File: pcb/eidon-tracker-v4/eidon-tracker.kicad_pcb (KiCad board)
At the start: 2 copper layers, 29.5 x 24.2 mm, 13 parts, among them SW1 SW_SPDT, U1 XIAO-ESP32C6-SMD, U2 BNO085

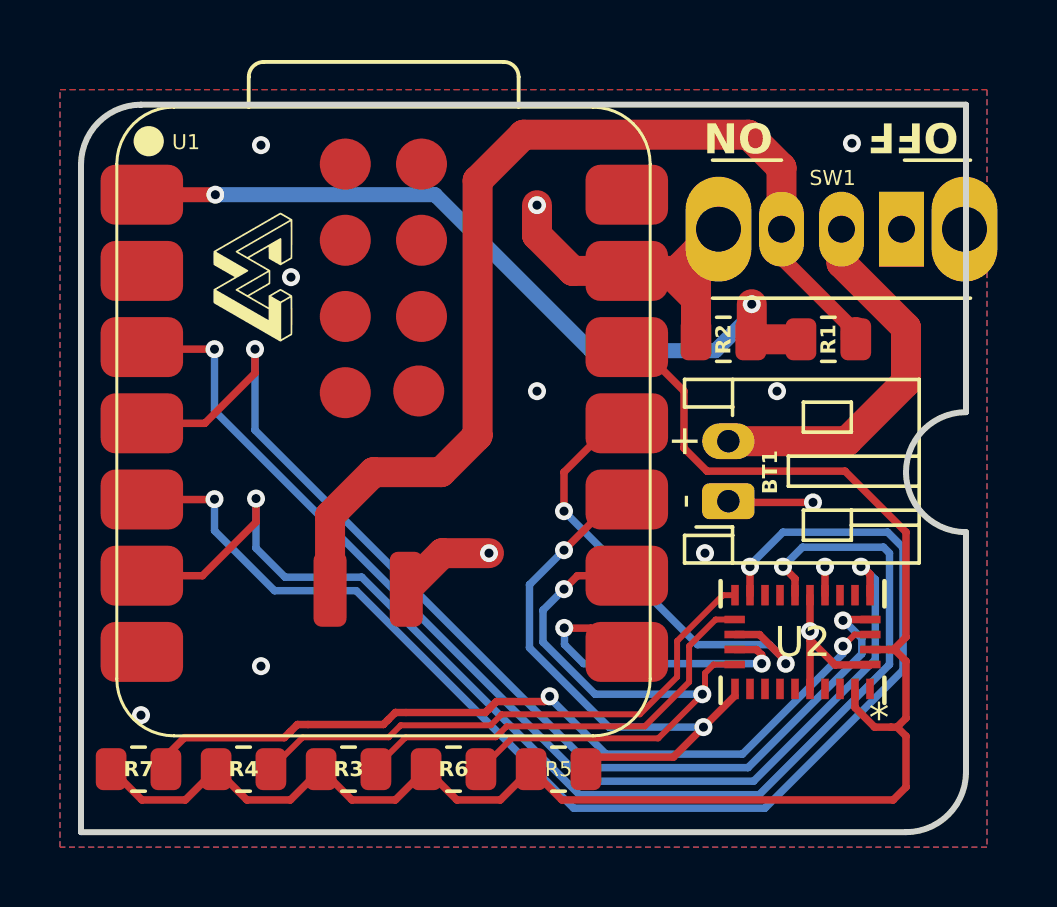
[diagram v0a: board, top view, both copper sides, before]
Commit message: feat(pcb): further refining traces for bno085 chip layout
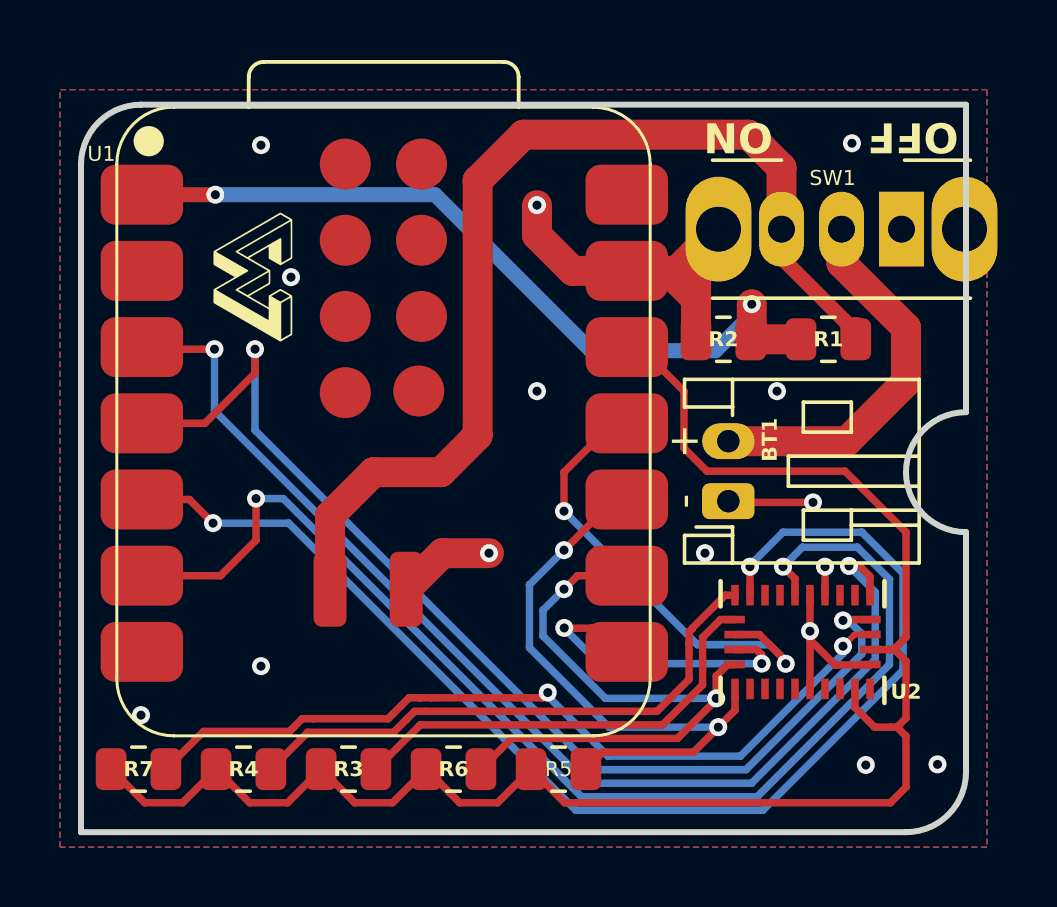
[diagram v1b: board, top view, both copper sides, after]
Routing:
- net /RST: track 42.1 -> 41.0 mm
- net /INT: track 43.0 -> 42.0 mm
- net /MISO: track 19.6 -> 20.4 mm
- net /SCK: track 20.7 -> 21.4 mm
- net /PS0: track 37.7 -> 38.3 mm
- net GND: vias 12 -> 14

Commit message: fix(pcb): corrects component placement so not too close to edge per jlcpcb rejection feedback
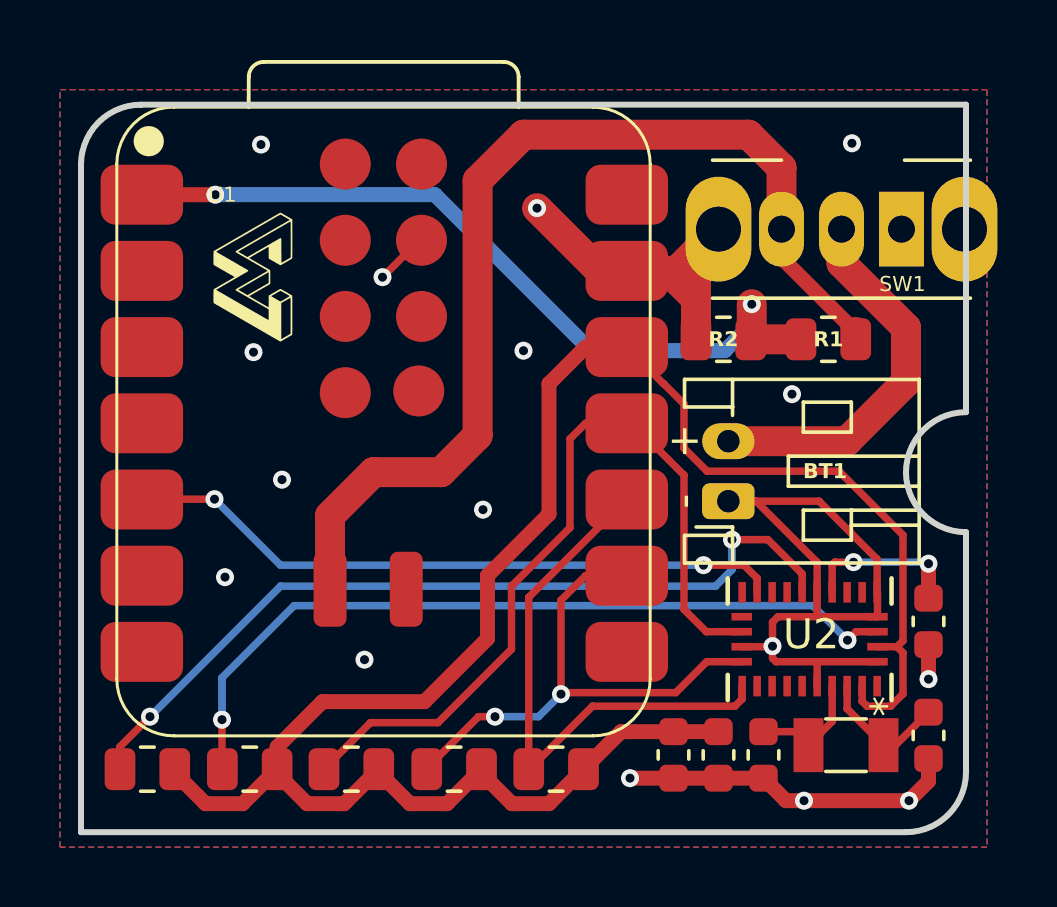
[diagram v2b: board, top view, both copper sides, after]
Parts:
- added C1: 22pF, Capacitor_SMD:C_0603_1608Metric, F.Cu at (162.2, 108.3)
- added C2: 22pF, Capacitor_SMD:C_0603_1608Metric, F.Cu at (156.8, 108.9)
- added C3: 100nF, Capacitor_SMD:C_0603_1608Metric, F.Cu at (162.2, 104.5)
- added C4: 100nF, Capacitor_SMD:C_0603_1608Metric, F.Cu at (155.2, 108.9)
- added C5: 100nF, Capacitor_SMD:C_0603_1608Metric, F.Cu at (153.8, 108.9)
- added X1: 32.768KHz, Crystal:Crystal_SMD_3215-2Pin_3.2x1.5mm, F.Cu at (159.5, 108.6)
- R5, R6: value 2.2k -> 10k
- U1: value XIAO-ESP32C6-SMD -> XIAO-ESP32-C6
- U2: footprint eidon-tracker:LGA-28_CEV -> eidon-tracker:BNO085
- moved R4 10.4 mm to (149.8, 109.4), turned to 0 degrees
- moved R5 10.3 mm to (139.6, 109.4), turned to 0 degrees
- moved R6 10.2 mm to (136.2, 109.4), turned to 0 degrees
- moved R7 7.10 mm to (143.0, 109.4), turned to 0 degrees
- moved R3 3.52 mm to (146.4, 109.4), turned to 0 degrees
- moved U2 0.26 mm to (158.3, 105.1)
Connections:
- R3 pad 1: Net-(U2-ENV_SDA) -> /SCL
- R4 pad 1: Net-(U2-ENV_SCL) -> /SDA
- R5 pad 1: /MISO -> /BOOTN
- R6 pad 1: /SCK -> /RST
- R7 pad 1: /BOOTN -> /SDO
- U1 pad 10: /MISO -> /SDA
- U1 pad 11: /MOSI -> /SDO
- U1 pad 14: (no net) -> unconnected-(U1-5V-Pad14)
- U1 pad 17: (no net) -> unconnected-(U1-MTDI-Pad17)
- U1 pad 18: (no net) -> unconnected-(U1-MTDO-Pad18)
- U1 pad 19: (no net) -> unconnected-(U1-EN-Pad19)
- U1 pad 20: (no net) -> GND
- U1 pad 21: (no net) -> unconnected-(U1-MTMS-Pad21)
- U1 pad 22: (no net) -> unconnected-(U1-MTCK-Pad22)
- U1 pad 23: /BOOT -> unconnected-(U1-BOOT-Pad23)
- U1 pad 24: (no net) -> unconnected-(U1-3V3_1-Pad24)
- U1 pad 3: /PS0 -> unconnected-(U1-GPIO2_A2_D2-Pad3)
- U1 pad 4: /PS1 -> unconnected-(U1-GPIO21_D3-Pad4)
- U1 pad 6: /RST -> unconnected-(U1-GPIO23_D5_SCL-Pad6)
- U1 pad 7: (no net) -> unconnected-(U1-GPIO16_D6_TX-Pad7)
- U1 pad 8: /CS -> unconnected-(U1-GPIO17_D7_RX-Pad8)
- U1 pad 9: /SCK -> /SCL
- U2 pad 15: Net-(U2-ENV_SCL) -> unconnected-(U2-ENV_SCL-Pad15)
- U2 pad 16: Net-(U2-ENV_SDA) -> unconnected-(U2-ENV_SDA-Pad16)
- U2 pad 17: /MOSI -> /SDO
- U2 pad 18: /CS -> GND
- U2 pad 19: /SCK -> /SCL
- U2 pad 20: /MISO -> /SDA
- U2 pad 26: unconnected-(U2-XOUT32/CLKSEL1-Pad26) -> /XOUT
- U2 pad 27: unconnected-(U2-XIN32-Pad27) -> /XIN
- U2 pad 5: /PS1 -> GND
- U2 pad 6: /PS0 -> GND
- U2 pad 9: unconnected-(U2-CAP-Pad9) -> /CAP
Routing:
- net /PS0: track 38.3 -> 0.00 mm, vias 2 -> 0
- net /PS1: track 37.0 -> 0.00 mm, vias 2 -> 0
- net /SDO: track 0.00 -> 27.3 mm
- net GND: track 28.0 -> 53.9 mm, vias 14 -> 16
- net /SCK: track 21.4 -> 0.00 mm, vias 2 -> 0
- net /MISO: track 20.4 -> 0.00 mm, vias 2 -> 0
- net /INT: track 42.0 -> 22.1 mm
- net /SDA: track 0.00 -> 18.9 mm
- net Net-(U2-ENV_SCL): track 18.8 -> 0.00 mm
- net /SCL: track 0.00 -> 18.0 mm, vias 0 -> 2
- net /MOSI: track 16.0 -> 0.00 mm, vias 2 -> 0
- net Net-(U2-ENV_SDA): track 15.0 -> 0.00 mm
- net /RST: track 41.0 -> 28.0 mm
- net /CS: track 10.9 -> 0.00 mm, vias 2 -> 0
- net VCC: track 56.2 -> 65.3 mm
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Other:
- board text removed: "OFF"
- board text removed: "ON"

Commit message: chore(pcb): commits hanging changes with final PCB design changes
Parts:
- R1, R2: value 220k -> 220kΩ
- R3, R4: value 2.2k -> 2.2kΩ
- R5, R6, R7: value 10k -> 10kΩ
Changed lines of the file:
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@@
 	(setup
 		(pad_to_mask_clearance 0.05)
-		(solder_mask_min_width 0.05)
 		(allow_soldermask_bridges_in_footprints no)
 		(tenting front back)
@@
 			)
 		)
-		(property "Value" "10k"
+		(property "Value" "10kΩ"
 			(at 0 1.65 0)
 			(layer "F.Fab")
@@
 			)
 		)
-		(property "Datasheet" "BNO085"
-			(at 0 0 270)
+		(property "Datasheet" "https://www.ceva-ip.com/wp-content/uploads/BNO080_085-Datasheet.pdf"
+			(at 0 0 90)
 			(layer "F.Fab")
 			(hide yes)
@@
 			)
 		)
-		(property "Description" ""
-			(at 0 0 270)
+		(property "Description" "9-Axis IMU Sensor Hub LGA-28"
+			(at 0 0 90)
 			(layer "F.Fab")
 			(hide yes)
@@
 			)
 		)
+		(property "Manufacturer" "CEVA Technologies"
+			(at 0 0 0)
+			(unlocked yes)
+			(layer "F.Fab")
+			(hide yes)
+			(effects
+				(font
+					(size 1 1)
+					(thickness 0.15)
+				)
+			)
+		)
+		(property "Manufacturer Part Number (MPN)" "BNO085"
+			(at 0 0 0)
+			(unlocked yes)
+			(layer "F.Fab")
+			(hide yes)
+			(effects
+				(font
+					(size 1 1)
+					(thickness 0.15)
+				)
+			)
+		)
+		(property "Supplier" "DigiKey"
+			(at 0 0 0)
+			(unlocked yes)
+			(layer "F.Fab")
+			(hide yes)
+			(effects
+				(font
+					(size 1 1)
+					(thickness 0.15)
+				)
+			)
+		)
+		(property "Supplier_PN" "1888-1006-1-ND"
+			(at 0 0 0)
+			(unlocked yes)
+			(layer "F.Fab")
+			(hide yes)
+			(effects
+				(font
+					(size 1 1)
+					(thickness 0.15)
+				)
+			)
+		)
 		(property ki_fp_filters "LGA-28_CEV")
 		(sheetname "/")
@@
 		)
 		(fp_text user "*"
-			(at 2.2356 -2.2625 270)
+			(at 2.2356 -2.2625 90)
 			(layer "F.SilkS")
 			(hide yes)
@@
 		)
 		(fp_text user "*"
-			(at 1.143 -2.2606 270)
+			(at 1.143 -2.2606 90)
 			(layer "F.Fab")
 			(hide yes)
@@
 			)
 		)
-		(property "Value" "10k"
+		(property "Value" "10kΩ"
 			(at 0 1.65 0)
 			(layer "F.Fab")
@@
 			)
 		)
-		(property "Value" "220k"
+		(property "Value" "220kΩ"
 			(at 0 0 90)
 			(layer "F.Fab")
@@
 			)
 		)
-		(property "Value" "220k"
+		(property "Value" "220kΩ"
 			(at 0 0 90)
 			(layer "F.Fab")
@@
 			)
 		)
-		(property "Value" "10k"
+		(property "Value" "10kΩ"
 			(at 0 1.65 0)
 			(layer "F.Fab")
@@
 			)
 		)
-		(property "Value" "2.2k"
+		(property "Value" "2.2kΩ"
 			(at 0 1.65 0)
 			(layer "F.Fab")
@@
 			)
 		)
-		(property "Value" "2.2k"
+		(property "Value" "2.2kΩ"
 			(at 0 1.65 0)
 			(layer "F.Fab")
@@
 			)
 		)
-		(property "Datasheet" ""
+		(property "Datasheet" "https://jlcpcb.com/api/file/downloadByFileSystemAccessId/8588897358871973888"
 			(at 0 0 180)
 			(unlocked yes)
@@
 			)
 		)
-		(property "Manufacturer Part Number (MPN)" "CK OS102011MA1Q"
+		(property "Manufacturer Part Number (MPN)" "CK OS102011MA1QN1"
 			(at 0 0 180)
 			(unlocked yes)
@@
 			)
 		)
-		(property "Supplier & Ref" "Mouser 611-OS102011MA1Q"
+		(property "Supplier & Ref" "LCSC C226259"
 			(at 0 0 180)
 			(unlocked yes)
